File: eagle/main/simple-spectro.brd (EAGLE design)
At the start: 99.1 x 73.7 mm, 55 parts, among them CON1 BAT, CON2 SPI, CON3 SPI, CON4 VIBR, IC1 32U4, IC2 MCP73831T, IC3 MCP1703CB, IC4 DMP1045U, Q6 BSP75, U1 NCT75DMR2G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

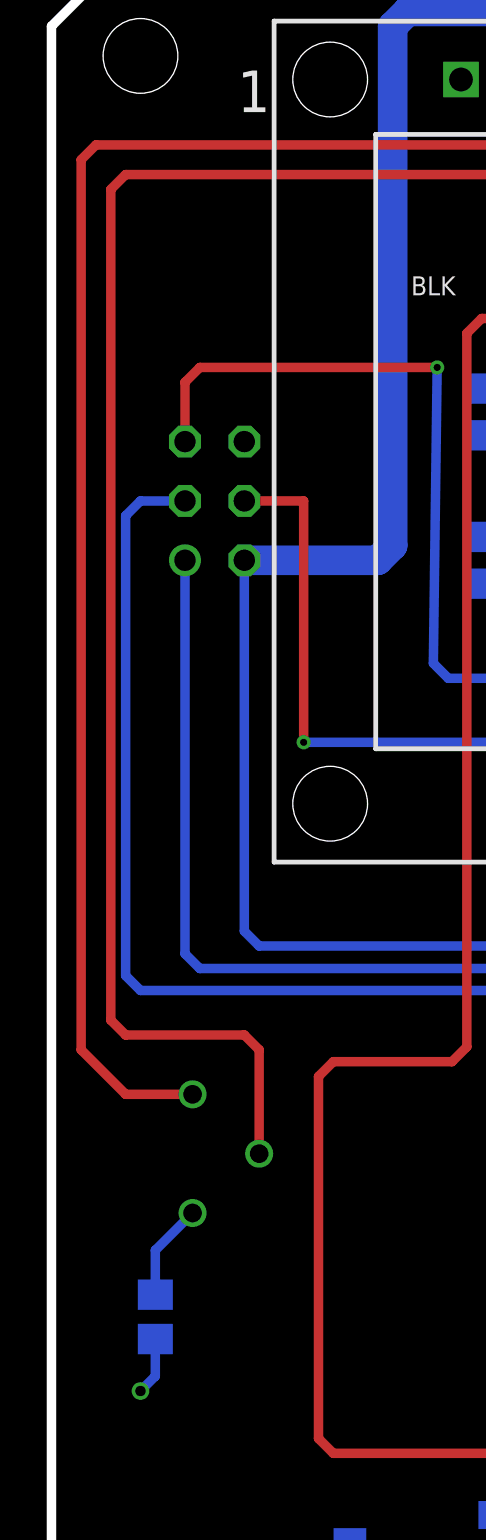
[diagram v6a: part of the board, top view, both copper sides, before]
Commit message: add second 100 ohms for constrast and marks for test
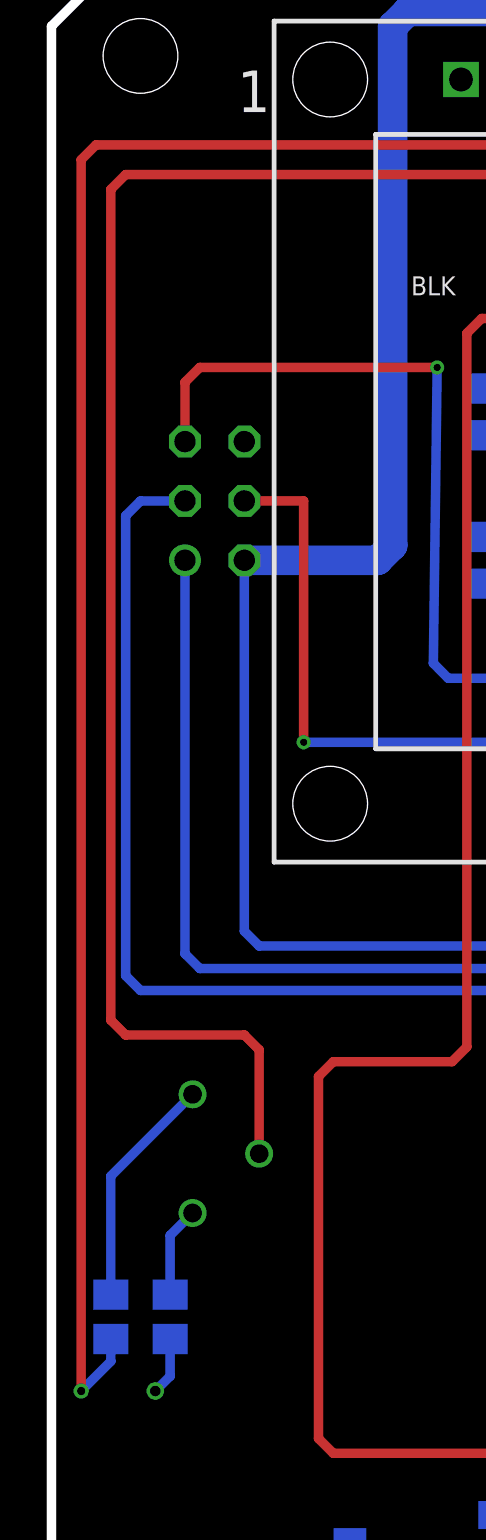
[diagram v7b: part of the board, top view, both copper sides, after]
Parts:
- added R14: 100, rcl:R0805
- moved R2 0.63 mm to (5.08, 15.9)
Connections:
- new net N$12: POT.3, R14.1
- net D13: now also R14.2; no longer POT.3
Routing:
- net D13: track 125.7 -> 137.5 mm, vias 1 -> 2
- net N$12: track 0.00 -> 10.0 mm
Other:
- board text added: "A"
- board text added: "B"
- board text added: "C"
- board text added: "D"
- board text added: "E"
- board text added: "F"
- board text added: "G"
- board text added: "H"
- board text added: "I"
- board text added: "J"
- board text added: "K"
- board text added: "L"
- board text added: "M"
- board text added: "N"
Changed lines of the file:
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@@
 <?xml version="1.0" encoding="utf-8"?>
 <!DOCTYPE eagle SYSTEM "eagle.dtd">
-<eagle version="8.4.0">
+<eagle version="9.0.0">
 <drawing>
 <settings>
@@
 <text x="57.21985" y="69.7484" size="1.27" layer="28" rot="MR0">GND</text>
 <text x="19.1008" y="69.7992" size="1.27" layer="28" rot="MR0">GND</text>
+<text x="71.12" y="48.895" size="1.778" layer="52" rot="MR0">C</text>
+<text x="86.36" y="59.055" size="1.778" layer="52" rot="MR0">A</text>
+<text x="86.995" y="64.77" size="1.778" layer="52" rot="MR0">B</text>
+<text x="62.23" y="36.83" size="1.778" layer="52" rot="MR0">D</text>
+<text x="55.245" y="66.04" size="1.778" layer="52" rot="MR0">E</text>
+<text x="52.07" y="66.04" size="1.778" layer="52" rot="MR0">F</text>
+<text x="49.53" y="66.04" size="1.778" layer="52" rot="MR0">G</text>
+<text x="46.99" y="66.04" size="1.778" layer="52" rot="MR0">H</text>
+<text x="44.45" y="66.04" size="1.778" layer="52" rot="MR0">I</text>
+<text x="31.115" y="66.04" size="1.778" layer="52" rot="MR0">J</text>
+<text x="28.575" y="66.04" size="1.778" layer="52" rot="MR0">K</text>
+<text x="26.035" y="66.04" size="1.778" layer="52" rot="MR0">L</text>
+<text x="23.495" y="66.04" size="1.778" layer="52" rot="MR0">M</text>
+<text x="20.955" y="66.04" size="1.778" layer="52" rot="MR0">N</text>
 </plain>
 <attributes>
@@
 <param name="dpMaxLengthDifference" value="10mm"/>
 <param name="dpGapFactor" value="2.5"/>
+<param name="checkAngle" value="0"/>
 <param name="checkFont" value="1"/>
 <param name="checkRestrict" value="0"/>
 <param name="checkStop" value="0"/>
+<param name="checkValues" value="0"/>
 <param name="useDiameter" value="13"/>
 <param name="maxErrors" value="50"/>
@@
 <attribute name="VALUE" x="64.77" y="43.815" size="1.27" layer="28" rot="MR90"/>
 </element>
-<element name="R2" library="rcl" package="R0805" value="100" x="4.445" y="15.875" rot="MR270">
-<attribute name="ELECROW" value="C17408" x="4.445" y="15.875" size="1.778" layer="28" rot="MR270" display="off"/>
-<attribute name="LCSC" value="C17408" x="4.445" y="15.875" size="1.778" layer="28" rot="MR270" display="off"/>
+<element name="R2" library="rcl" package="R0805" value="100" x="5.08" y="15.875" rot="MR270">
+<attribute name="ELECROW" value="C17408" x="5.08" y="15.875" size="1.778" layer="28" rot="MR270" display="off"/>
+<attribute name="LCSC" value="C17408" x="5.08" y="15.875" size="1.778" layer="28" rot="MR270" display="off"/>
 </element>
 <element name="R13" library="rcl" package="R0805" value="10k" x="69.215" y="61.595" rot="MR90">
@@
 <attribute name="LCSC" value="C79709" x="83.82" y="37.465" size="1.778" layer="28" rot="MR90" display="off"/>
 </element>
+<element name="R14" library="rcl" package="R0805" value="100" x="2.54" y="15.875" rot="MR270">
+<attribute name="ELECROW" value="C17408" x="2.54" y="15.875" size="1.778" layer="28" rot="MR270" display="off"/>
+<attribute name="LCSC" value="C17408" x="2.54" y="15.875" size="1.778" layer="28" rot="MR270" display="off"/>
+</element>
 </elements>
 <signals>
@@
 <wire x1="79.06" y1="69.53" x2="80.645" y2="69.53" width="0.8128" layer="16"/>
 <contactref element="R2" pad="2"/>
-<wire x1="4.445" y1="14.925" x2="4.445" y2="13.335" width="0.4064" layer="16"/>
-<wire x1="4.445" y1="13.335" x2="3.81" y2="12.7" width="0.4064" layer="16"/>
-<via x="3.81" y="12.7" extent="1-16" drill="0.45"/>
+<wire x1="5.08" y1="14.925" x2="5.08" y2="13.335" width="0.4064" layer="16"/>
+<wire x1="5.08" y1="13.335" x2="4.445" y2="12.7" width="0.4064" layer="16"/>
+<via x="4.445" y="12.7" extent="1-16" drill="0.45"/>
 <via x="49.89195" y="59.37" extent="1-16" drill="0.35"/>
 <wire x1="48.31" y1="59.37" x2="49.89195" y2="59.37" width="0.4064" layer="16"/>
@@
 <wire x1="52.705" y1="61.595" x2="53.34" y2="62.23" width="0.4064" layer="16"/>
 <wire x1="53.34" y1="63.82" x2="53.34" y2="62.23" width="0.4064" layer="16"/>
-<contactref element="POT" pad="3"/>
-<wire x1="6.04" y1="25.4" x2="3.175" y2="25.4" width="0.4064" layer="1"/>
-<wire x1="3.175" y1="25.4" x2="1.27" y2="27.305" width="0.4064" layer="1"/>
-<wire x1="1.27" y1="27.305" x2="1.27" y2="65.405" width="0.4064" layer="1"/>
-<wire x1="1.27" y1="65.405" x2="1.905" y2="66.04" width="0.4064" layer="1"/>
+<wire x1="1.905" y1="66.04" x2="1.27" y2="65.405" width="0.4064" layer="1"/>
 <wire x1="19.685" y1="66.04" x2="20.07" y2="66.425" width="0.4064" layer="1"/>
 <wire x1="20.07" y1="66.425" x2="20.07" y2="68.84" width="0.4064" layer="1"/>
@@
 <wire x1="51.7779" y1="69.5071" x2="51.7779" y2="63.7794" width="0.4064" layer="1"/>
 <wire x1="1.905" y1="66.04" x2="19.685" y2="66.04" width="0.4064" layer="1"/>
+<contactref element="R14" pad="2"/>
+<via x="1.27" y="12.7" extent="1-16" drill="0.35"/>
+<wire x1="1.27" y1="12.7" x2="2.54" y2="13.97" width="0.4064" layer="16"/>
+<wire x1="2.54" y1="13.97" x2="2.54" y2="14.925" width="0.4064" layer="16"/>
+<wire x1="1.27" y1="65.405" x2="1.27" y2="12.7" width="0.4064" layer="1"/>
 </signal>
 <signal name="D8">
@@
 <contactref element="POT" pad="1"/>
 <contactref element="R2" pad="1"/>
-<wire x1="4.445" y1="16.825" x2="4.445" y2="18.725" width="0.4064" layer="16"/>
-<wire x1="4.445" y1="18.725" x2="6.04" y2="20.32" width="0.4064" layer="16"/>
+<wire x1="5.08" y1="16.825" x2="5.08" y2="19.36" width="0.4064" layer="16"/>
+<wire x1="5.08" y1="19.36" x2="6.04" y2="20.32" width="0.4064" layer="16"/>
 </signal>
 <signal name="N$5">
@@
 <wire x1="69.215" y1="62.865" x2="69.215" y2="62.545" width="0.4064" layer="16"/>
 </signal>
+<signal name="N$12">
+<contactref element="R14" pad="1"/>
+<contactref element="POT" pad="3"/>
+<wire x1="2.54" y1="16.825" x2="2.54" y2="21.9" width="0.4064" layer="16"/>
+<wire x1="2.54" y1="21.9" x2="6.04" y2="25.4" width="0.4064" layer="16"/>
+</signal>
 </signals>
-<errors>
-</errors>
 </board>
 </drawing>
